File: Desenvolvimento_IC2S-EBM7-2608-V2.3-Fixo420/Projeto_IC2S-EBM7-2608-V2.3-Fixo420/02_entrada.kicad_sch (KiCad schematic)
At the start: 9 parts, among them T1 TP_+24V, T2 TP_GND_ADC_P1

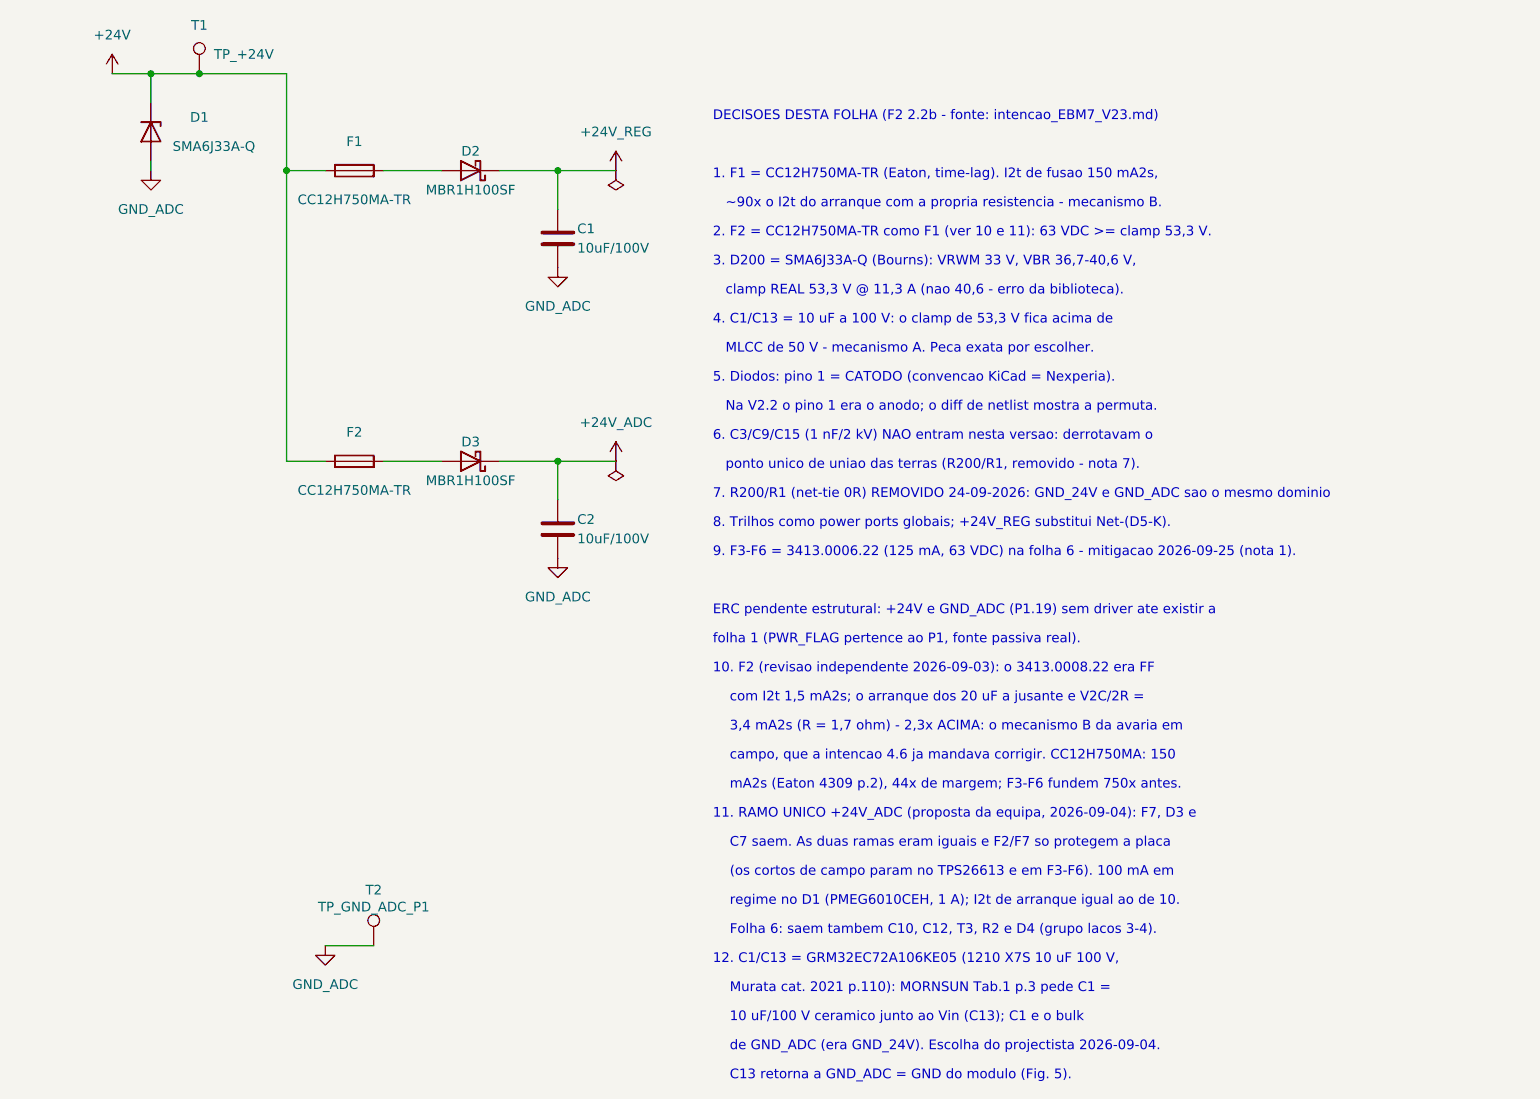
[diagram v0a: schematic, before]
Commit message: Revisao da reuniao 28-09: ramo unico de 24 V, 100 nF a 50 V, um so MPN de 1 uF
- Saem F2, o diodo e o condensador do ramo +24V_ADC; F1 + diodo alimentam o
  R-78HB e o +24V_ADC. +24V_REG deixa de existir (esquematico, PCB, netclasses).
- Condensador de entrada do R-78HB conferido contra o datasheet Recom (p.4):
  10 uF/100 V cumpre os 3,3 uF/100 V pedidos com Vin > 50 V. Sem alteracao.
- 100 nF fora do 24 V -> TDK C1608X7R1H104K080AA (50 V); o do +24V_ADC fica
  GRM188R72A104KA35D (100 V). 1 uF -> TDK C1608X7R1H105K080AB nos quatro.
- Notas 2, 13 e 14 da folha 2; README e registo em 00-Especificacoes;
  catalogo TDK em Documentos_de_Referencia.

Co-Authored-By: Claude Opus 5.5 (1M context) <noreply@anthropic.com>
Claude-Session: https://claude.ai/code/session_01KPnkiJQKrkjgRqqw9M78ie
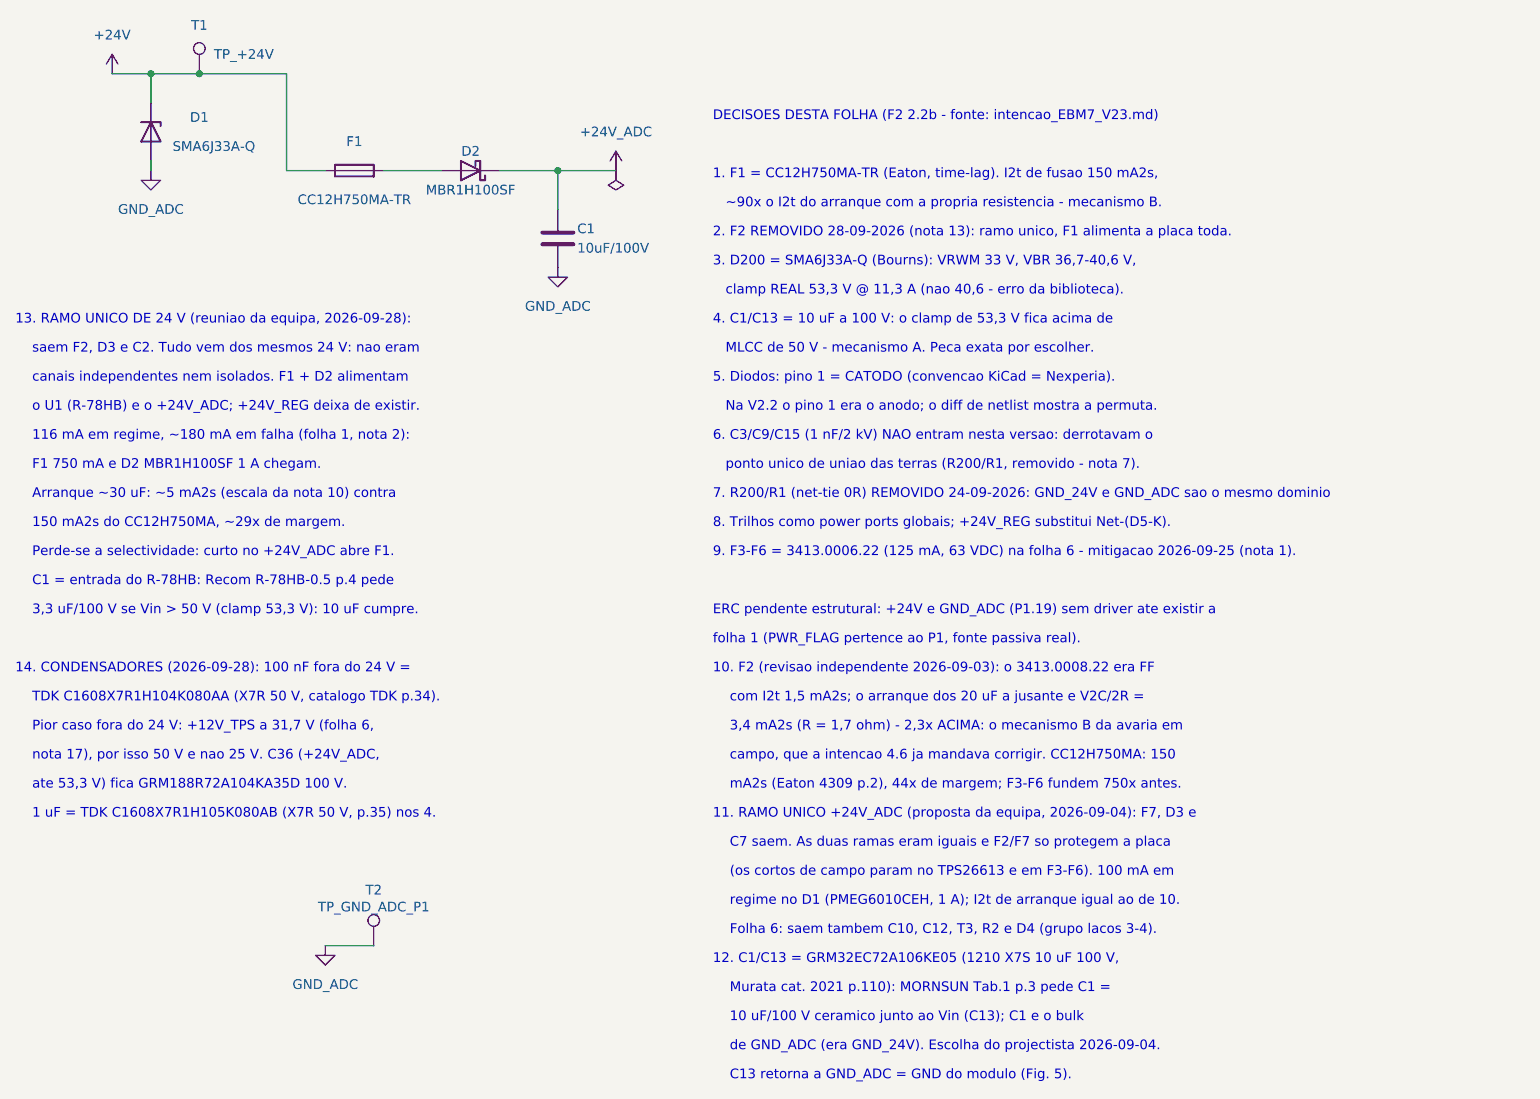
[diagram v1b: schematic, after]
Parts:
- removed C2: 10uF/100V, EBM7_V23:C_1210_3225Metric, symbol Device:C
- removed D3: MBR1H100SF, EBM7_V23:SOD123, symbol Device:D_Schottky
- removed F2: CC12H750MA-TR, EBM7_V23:1206F, symbol Device:Fuse
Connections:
- net +24V_REG is gone; now on net +24V_ADC: C1.1, D2.1 (K)
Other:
- note added: "1 uF = TDK C1608X7R1H105K080AB (X7R 50 V, p.35) nos 4."
- note added: "116 mA em regime, ~180 mA em falha (folha 1, nota 2):"
- note added: "13. RAMO UNICO DE 24 V (reuniao da equipa, 2026-09-28):"
- note added: "14. CONDENSADORES (2026-09-28): 100 nF fora do 24 V ="
- note added: "150 mA2s do CC12H750MA, ~29x de margem."
- note added: "2. F2 REMOVIDO 28-09-2026 (nota 13): ramo unico, F1 alimenta a placa toda."
- note added: "3,3 uF/100 V se Vin > 50 V (clamp 53,3 V): 10 uF cumpre."
- note added: "Arranque ~30 uF: ~5 mA2s (escala da nota 10) contra"
- note added: "C1 = entrada do R-78HB: Recom R-78HB-0.5 p.4 pede"
- note added: "F1 750 mA e D2 MBR1H100SF 1 A chegam."
- note added: "Perde-se a selectividade: curto no +24V_ADC abre F1."
- note added: "Pior caso fora do 24 V: +12V_TPS a 31,7 V (folha 6,"
- note added: "TDK C1608X7R1H104K080AA (X7R 50 V, catalogo TDK p.34)."
- note added: "ate 53,3 V) fica GRM188R72A104KA35D 100 V."
- note added: "canais independentes nem isolados. F1 + D2 alimentam"
- note added: "nota 17), por isso 50 V e nao 25 V. C36 (+24V_ADC,"
- note added: "o U1 (R-78HB) e o +24V_ADC; +24V_REG deixa de existir."
- note added: "saem F2, D3 e C2. Tudo vem dos mesmos 24 V: nao eram"
- note removed: "2. F2 = CC12H750MA-TR como F1 (ver 10 e 11): 63 VDC >= clamp 53,3 V."
